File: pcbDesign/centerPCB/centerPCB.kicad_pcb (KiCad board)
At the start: 2 copper layers, 157 x 58.8 mm, 7 parts, among them J1 Conn_01x07_Pin, J2 Conn_01x12_Pin

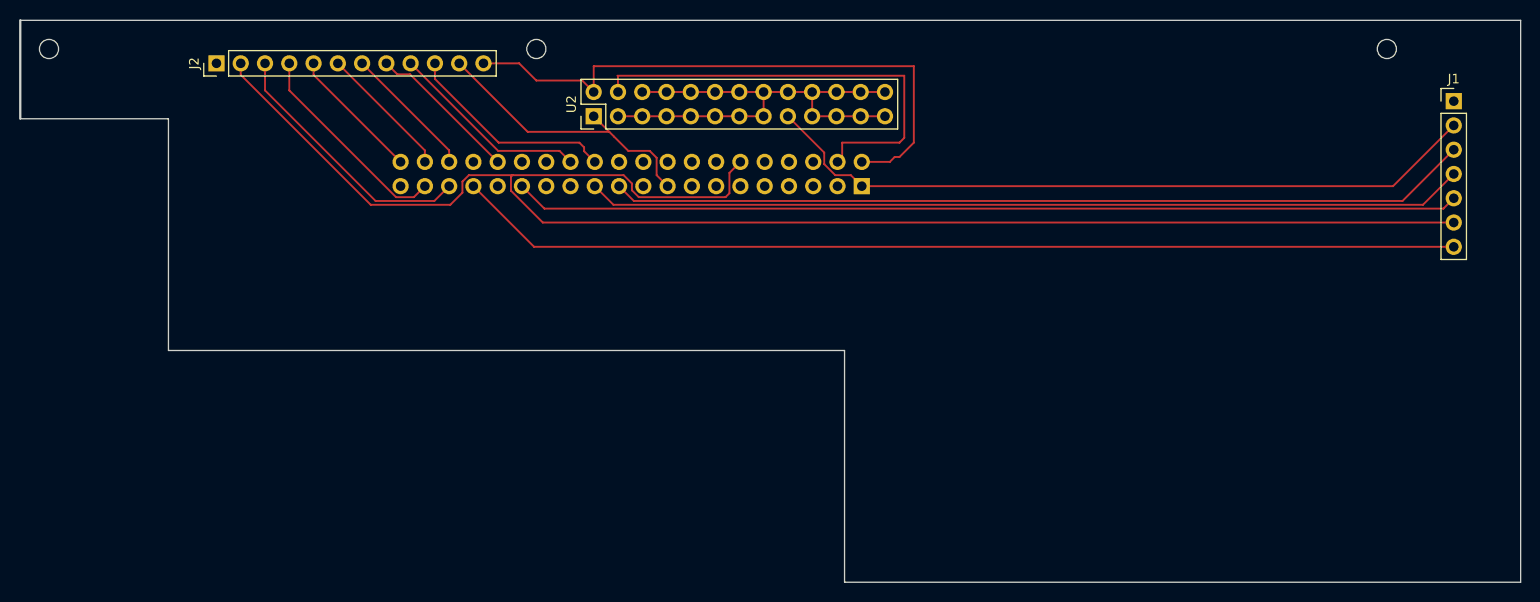
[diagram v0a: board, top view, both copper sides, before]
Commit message: Updated pcbs and added footprint for rotary encoder (in progress)
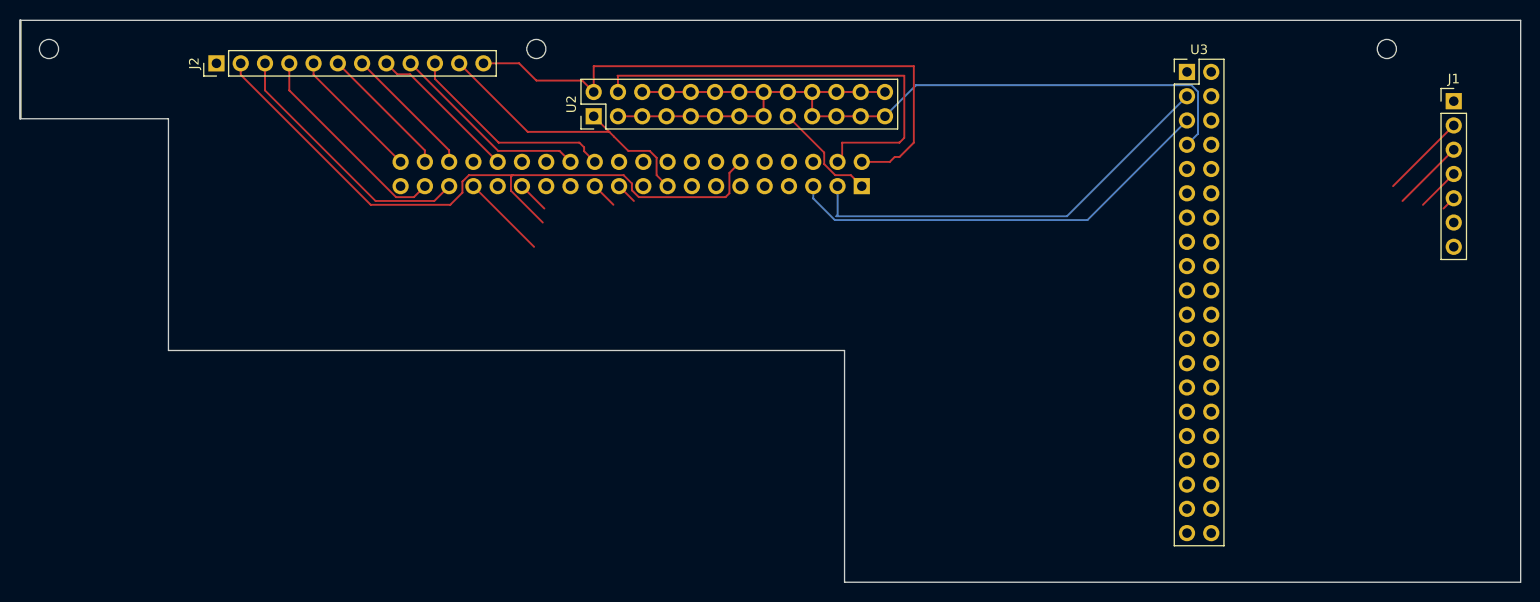
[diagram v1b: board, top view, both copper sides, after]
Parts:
- added U3: ~, Connector_PinHeader_2.54mm:PinHeader_2x20_P2.54mm_Vertical, F.Cu at (180.1, 58.1)
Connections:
- U1 pad 27: GND -> /EEPROM SDA
- U1 pad 28: GND -> /EEPROM SDL
- U1 pad 3: GND -> /MCU SDA
- U1 pad 5: GND -> /MCU SCL
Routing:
- net /Brightness_DT: track 105.2 -> 8.97 mm
- net /Clk: track 167.0 -> 71.6 mm
- net /1: track 98.9 -> 4.86 mm
- net /2: track 92.0 -> 7.32 mm
- net /Start: track 90.2 -> 9.78 mm
- net /3v3: track 106.6 -> 51.0 mm
- net /MCU SCL: track 0.00 -> 45.6 mm
- net /MCU SDA: track 0.00 -> 45.1 mm
- net GND: track 53.3 -> 93.8 mm

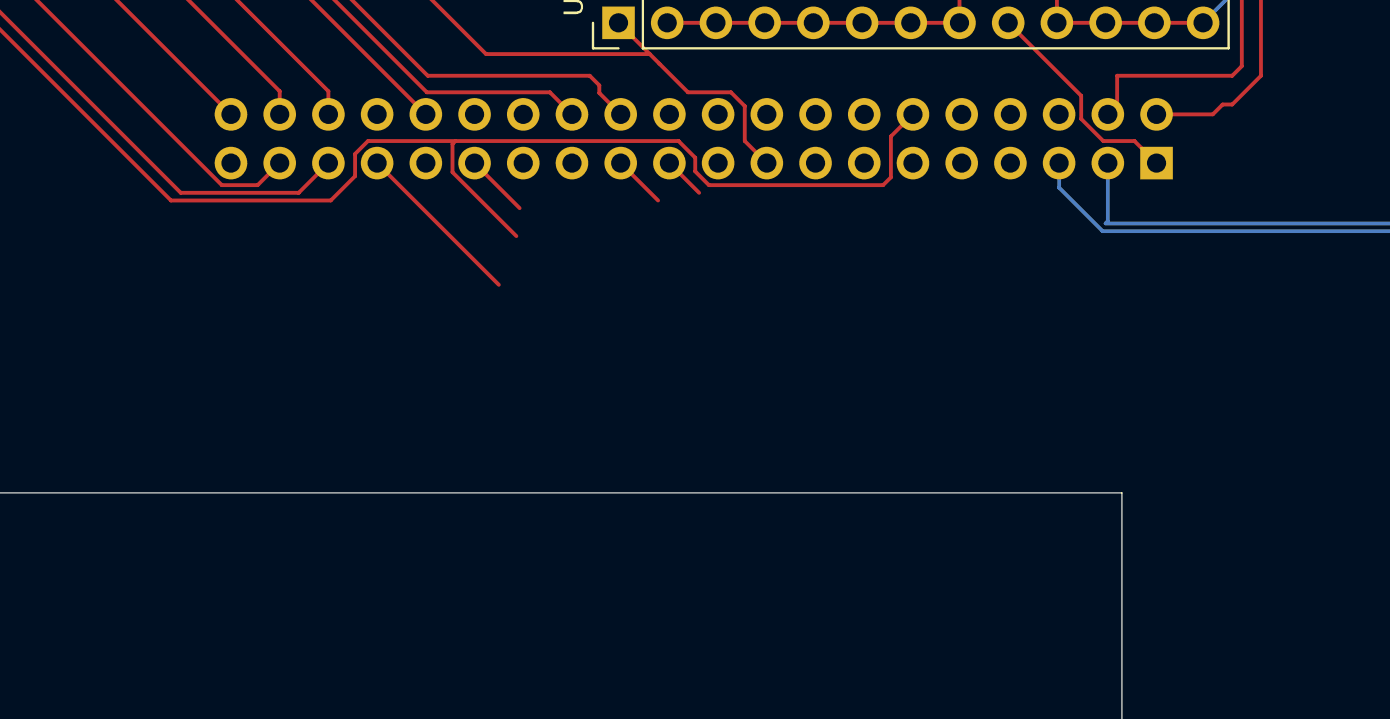
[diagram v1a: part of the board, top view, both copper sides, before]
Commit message: finalized center pcb component placement
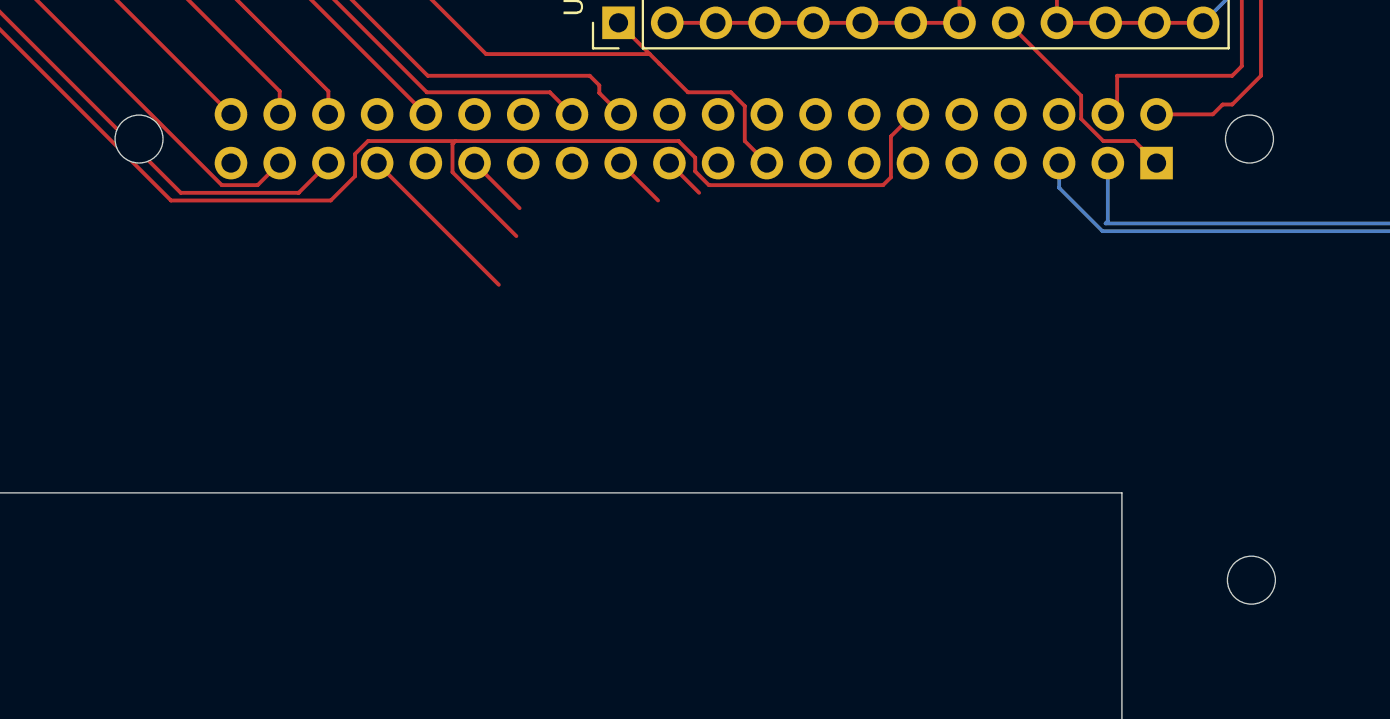
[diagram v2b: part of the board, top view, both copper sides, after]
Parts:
- added ?: , , F.Cu at (151.0, 91.8)
- added ?: , , F.Cu at (93.0, 68.8)
- added ?: , , F.Cu at (150.9, 68.8)
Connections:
- net /Brightness_DT renamed /Brightness_A
- J1 pad 6: /Clk -> /Brightness_B
- J2 pad 2: /Clk -> /Volume_B
- J2 pad 4: /Volume_DT -> /Volume_A
- U1 pad 12: /Clk -> /Volume_B
- U1 pad 37: /Volume_DT -> /Volume_B
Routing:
- net /Volume_B: track 0.00 -> 93.8 mm
- net /Clk: track 71.6 -> 0.00 mm
- net /Volume_DT: track 22.1 -> 0.00 mm

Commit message: routed centerpcb
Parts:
- removed ? (x6): , 
- added H1: MountingHole, MountingHole:MountingHole_2.1mm, F.Cu at (61.0, 55.7)
- added H2: MountingHole, MountingHole:MountingHole_2.1mm, F.Cu at (112.0, 55.7)
- added H3: MountingHole, MountingHole:MountingHole_2.1mm, F.Cu at (201.0, 55.7)
- added H4: MountingHole, MountingHole:MountingHole_2.5mm, F.Cu at (151.0, 91.8)
- added H5: MountingHole, MountingHole:MountingHole_2.5mm, F.Cu at (93.0, 68.8)
- added H6: MountingHole, MountingHole:MountingHole_2.5mm, F.Cu at (150.9, 68.8)
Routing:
- net GND: track 93.8 -> 299.2 mm
- net /Brightness_A: track 8.97 -> 105.4 mm
- net /1: track 4.86 -> 99.4 mm
- net /EEPROM SDL: track 0.00 -> 90.8 mm, vias 0 -> 1
- net /3v3: track 51.0 -> 141.4 mm, vias 0 -> 1
- net /EEPROM SDA: track 0.00 -> 85.4 mm, vias 0 -> 1
- net /2: track 7.32 -> 92.2 mm
- net /Start: track 9.78 -> 90.4 mm
- net /Volume_B: track 93.8 -> 62.1 mm
- net /5v: track 110.4 -> 99.7 mm
- net /MCU SCL: track 45.6 -> 42.1 mm
- net /LR_Clk: track 27.5 -> 24.9 mm
- net /MCU SDA: track 45.1 -> 42.7 mm, vias 0 -> 1
- net /Power_LED: track 22.2 -> 21.2 mm
- net /D_In: track 14.1 -> 14.7 mm
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- added copper zone on In1.Cu, net GND
- added copper zone on In2.Cu, net GND
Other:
- copper layers 2 -> 4
